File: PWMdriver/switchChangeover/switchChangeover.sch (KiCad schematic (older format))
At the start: 7 parts

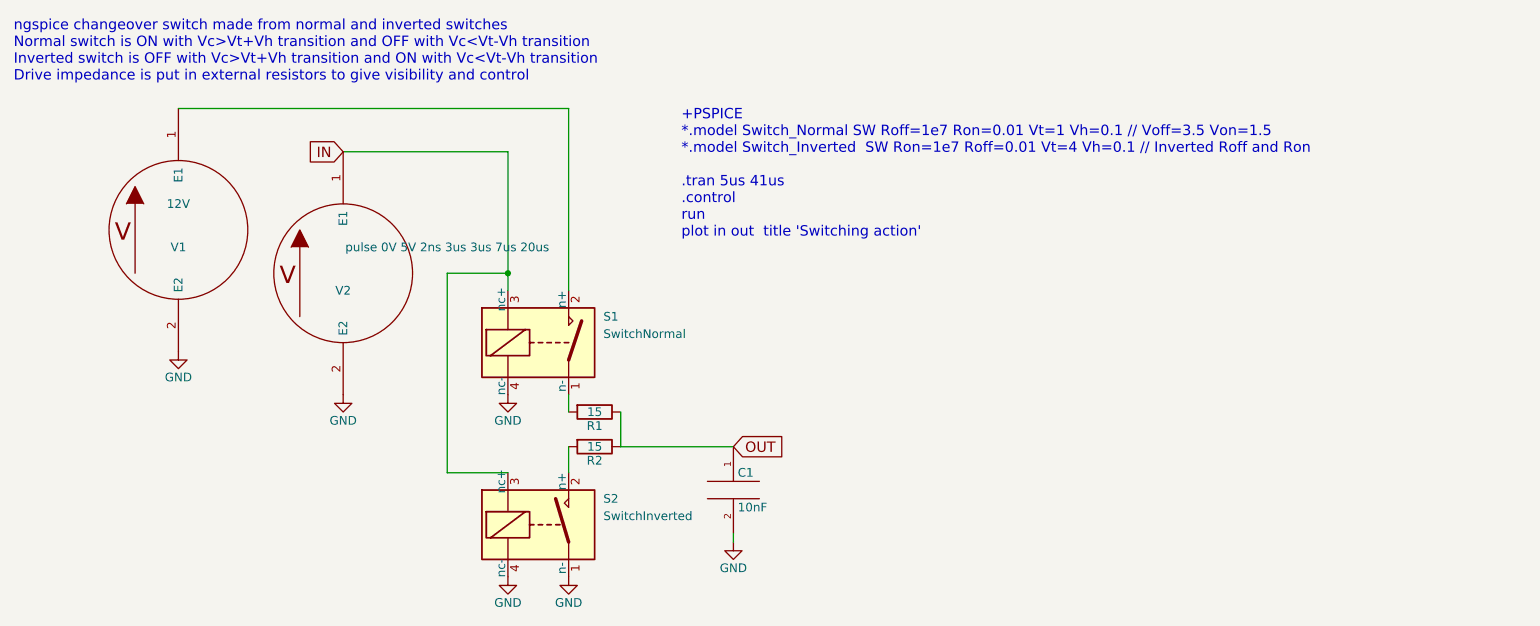
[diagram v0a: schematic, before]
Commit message: Updated to use NO and NC switches
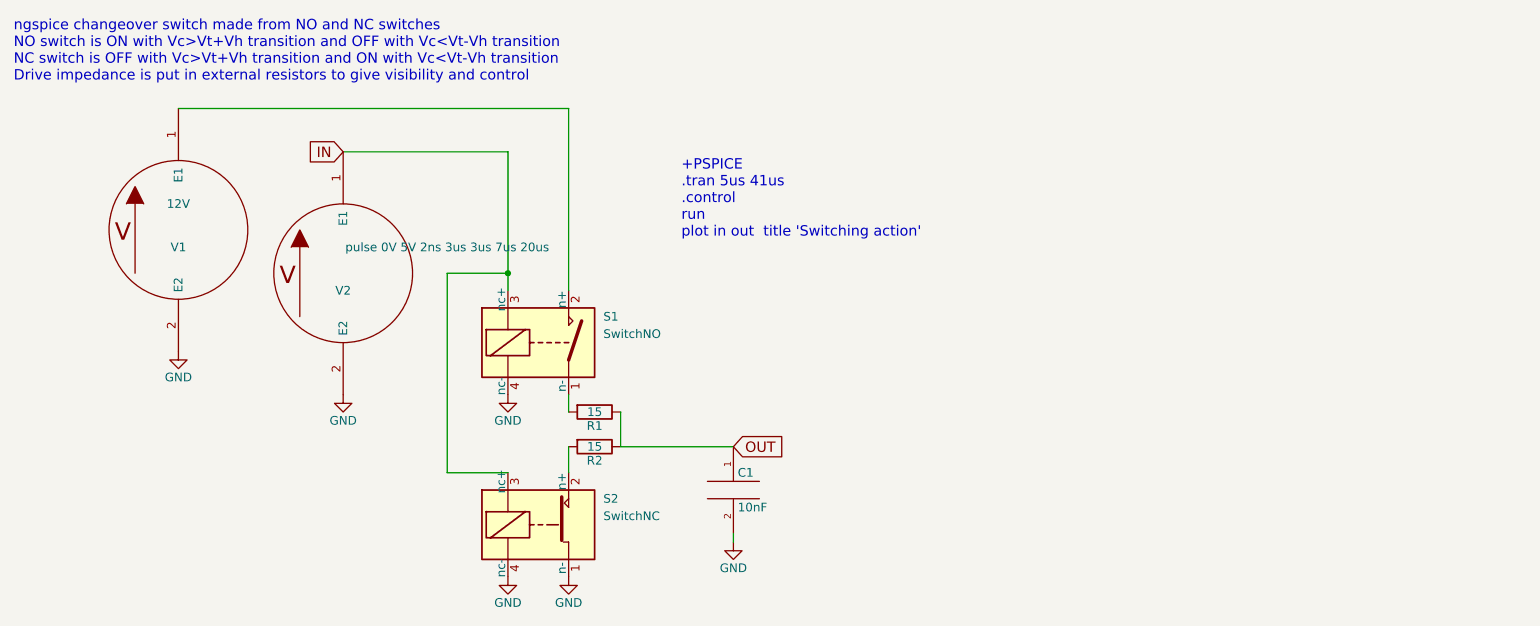
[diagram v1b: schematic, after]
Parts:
- removed S1: SwitchNormal, switchSpice, symbol SwitchNormal
- removed S2: SwitchInverted, switchSpice, symbol SwitchInverted
- added S1: SwitchNO, switchSpice, symbol SwitchNO
- added S2: SwitchNC, switchSpice, symbol SwitchNC
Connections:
- net GND: now also S1.4 (nc-), S2.1 (n-), S2.4 (nc-)
- net IN: now also S1.3 (nc+), S2.3 (nc+)
- net at R2.2: now also S2.2 (n+)
- net at V1.1 (E1): now also S1.2 (n+)
- net at R1.2: now also S1.1 (n-)
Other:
- note added: "+PSPICE\n.tran 5us 41us\n.control \nrun\nplot in out title 'Switching action'\n"
- note added: "ngspice changeover switch made from NO and NC switches\nNO switch is ON with Vc>Vt+Vh transition and OFF with Vc<Vt-Vh transition\nNC switch is OFF with Vc>Vt+Vh transition and ON with Vc<Vt-Vh transition\nDrive impedance is put in external resistors to give visibility and control"
- note removed: "+PSPICE\n*.model Switch_Normal SW Roff=1e7 Ron=0.01 Vt=1 Vh=0.1 // Voff=3.5 Von=1.5\n*.model Switch_Inverted SW Ron=1e7 Roff=0.01 Vt=4 Vh=0.1 // Inverted Roff and Ron\n\n.tran 5us 41us\n.control \nrun\nplot in out title 'Switching action'\n"
- note removed: "ngspice changeover switch made from normal and inverted switches\nNormal switch is ON with Vc>Vt+Vh transition and OFF with Vc<Vt-Vh transition\nInverted switch is OFF with Vc>Vt+Vh transition and ON with Vc<Vt-Vh transition\nDrive impedance is put in external resistors to give visibility and control"
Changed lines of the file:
@@
 $EndDescr
 $Comp
-L GND #PWR01
+L GND #PWR3
 U 1 1 5B0DBA73
 P 3650 2800
-F 0 "#PWR01" H 3650 2550 50  0001 C CNN
+F 0 "#PWR3" H 3650 2550 50  0001 C CNN
 F 1 "GND" H 3650 2650 50  0000 C CNN
 F 2 "" H 3650 2800 50  0001 C CNN
@@
 $EndComp
 $Comp
-L GND #PWR02
+L GND #PWR2
 U 1 1 5B0DBA75
 P 2700 2800
-F 0 "#PWR02" H 2700 2550 50  0001 C CNN
+F 0 "#PWR2" H 2700 2550 50  0001 C CNN
 F 1 "GND" H 2700 2650 50  0000 C CNN
 F 2 "" H 2700 2800 50  0001 C CNN
@@
 IN
 Text Notes 4650 1900 0    60   ~ 0
-+PSPICE\n*.model Switch_Normal SW Roff=1e7 Ron=0.01 Vt=1 Vh=0.1 // Voff=3.5 Von=1.5\n*.model Switch_Inverted  SW Ron=1e7 Roff=0.01 Vt=4 Vh=0.1 // Inverted Roff and Ron\n\n.tran 5us 41us\n.control \nrun\nplot in out  title 'Switching action'\n
++PSPICE\n.tran 5us 41us\n.control \nrun\nplot in out  title 'Switching action'\n
 Wire Wire Line
 	3650 1400 3650 2200
@@
 $EndComp
 $Comp
-L GND #PWR03
+L GND #PWR1
 U 1 1 5B0DBA7A
 P 1750 2550
-F 0 "#PWR03" H 1750 2300 50  0001 C CNN
+F 0 "#PWR1" H 1750 2300 50  0001 C CNN
 F 1 "GND" H 1750 2400 50  0000 C CNN
 F 2 "" H 1750 2550 50  0001 C CNN
@@
 	3300 2100 3650 2100
 Text Notes 800  1000 0    60   ~ 0
-ngspice changeover switch made from normal and inverted switches\nNormal switch is ON with Vc>Vt+Vh transition and OFF with Vc<Vt-Vh transition\nInverted switch is OFF with Vc>Vt+Vh transition and ON with Vc<Vt-Vh transition\nDrive impedance is put in external resistors to give visibility and control
+ngspice changeover switch made from NO and NC switches\nNO switch is ON with Vc>Vt+Vh transition and OFF with Vc<Vt-Vh transition\nNC switch is OFF with Vc>Vt+Vh transition and ON with Vc<Vt-Vh transition\nDrive impedance is put in external resistors to give visibility and control
 Wire Wire Line
 	3650 3250 3300 3250
@@
 	3300 3250 3300 2100
 $Comp
-L GND #PWR04
+L GND #PWR5
 U 1 1 5B0DBC43
 P 3650 3850
-F 0 "#PWR04" H 3650 3600 50  0001 C CNN
+F 0 "#PWR5" H 3650 3600 50  0001 C CNN
 F 1 "GND" H 3650 3700 50  0000 C CNN
 F 2 "" H 3650 3850 50  0001 C CNN
@@
 $EndComp
 $Comp
-L GND #PWR05
+L GND #PWR6
 U 1 1 5B0DBC60
 P 4000 3850
-F 0 "#PWR05" H 4000 3600 50  0001 C CNN
+F 0 "#PWR6" H 4000 3600 50  0001 C CNN
 F 1 "GND" H 4000 3700 50  0000 C CNN
 F 2 "" H 4000 3850 50  0001 C CNN
@@
 $EndComp
 $Comp
-L GND #PWR06
+L GND #PWR4
 U 1 1 5B0DBE76
 P 4950 3650
-F 0 "#PWR06" H 4950 3400 50  0001 C CNN
+F 0 "#PWR4" H 4950 3400 50  0001 C CNN
 F 1 "GND" H 4950 3500 50  0000 C CNN
 F 2 "" H 4950 3650 50  0001 C CNN
 F 3 "" H 4950 3650 50  0001 C CNN
 	1    4950 3650
-	1    0    0    -1
-$EndComp
-$Comp
-L SwitchInverted S2
-U 1 1 5B0D530B
-P 3850 3550
-F 0 "S2" H 4200 3700 50  0000 L CNN
-F 1 "SwitchInverted" H 4200 3600 50  0000 L CNN
-F 2 "switchSpice" H 5120 3520 50  0001 C CNN
-F 3 "" H 3850 3550 50  0001 C CNN
-	1    3850 3550
 	1    0    0    -1
 $EndComp
@@
 $EndBitmap
 $Comp
-L SwitchNormal S1
-U 1 1 5B0E5629
+L SwitchNO S1
+U 1 1 5B14E779
 P 3850 2500
 F 0 "S1" H 4200 2650 50  0000 L CNN
-F 1 "SwitchNormal" H 4200 2550 50  0000 L CNN
+F 1 "SwitchNO" H 4200 2550 50  0000 L CNN
 F 2 "switchSpice" H 5120 2470 50  0001 C CNN
 F 3 "" H 3850 2500 50  0001 C CNN
@@
 	1    0    0    -1
 $EndComp
+$Comp
+L SwitchNC S2
+U 1 1 5B14E7D4
+P 3850 3550
+F 0 "S2" H 4200 3700 50  0000 L CNN
+F 1 "SwitchNC" H 4200 3600 50  0000 L CNN
+F 2 "switchSpice" H 5120 3520 50  0001 C CNN
+F 3 "" H 3850 3550 50  0001 C CNN
+	1    3850 3550
+	1    0    0    -1
+$EndComp
